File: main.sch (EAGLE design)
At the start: 45 parts, among them IC1 ATTINY13A-SSH, IC2 TP4056-42-ESOP8, IC3 LM27313XMFX_NOPB, IC4 TPL5110DDCT, IC5 ATTINY13A-SSH, T1A 2N4401, T1B NPN, X1 MINI-USB-UX60A-MB-5ST, X2 332-02

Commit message: updates
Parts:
- added R15: 0R, resistor:R-EU_R0402
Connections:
- new net N$16: IC5.PB0, R15.1
- net SOLAR_REG+/-: now also R15.2; no longer IC5.PB0
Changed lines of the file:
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@@
 <?xml version="1.0" encoding="utf-8"?>
 <!DOCTYPE eagle SYSTEM "eagle.dtd">
-<eagle version="9.5.2">
+<eagle version="9.6.0">
 <drawing>
 <settings>
@@
 <part name="GND4" library="supply1" library_urn="urn:adsk.eagle:library:371" deviceset="GND" device=""/>
 <part name="R14" library="resistor" library_urn="urn:adsk.eagle:library:348" deviceset="R-EU_" device="R0402" package3d_urn="urn:adsk.eagle:package:26058/1" value="0R"/>
+<part name="R15" library="resistor" library_urn="urn:adsk.eagle:library:348" deviceset="R-EU_" device="R0402" package3d_urn="urn:adsk.eagle:package:26058/1" value="0R"/>
 </parts>
 <sheets>
@@
 <attribute name="VALUE" x="163.83" y="59.182" size="1.778" layer="96" rot="R180"/>
 </instance>
+<instance part="R15" gate="G$1" x="170.18" y="58.42" smashed="yes" rot="R180">
+<attribute name="NAME" x="168.91" y="62.0014" size="1.778" layer="95" rot="R180"/>
+<attribute name="VALUE" x="173.99" y="61.722" size="1.778" layer="96" rot="R180"/>
+</instance>
 </instances>
 <busses>
@@
 <junction x="91.44" y="63.5"/>
 <junction x="91.44" y="58.42"/>
-<pinref part="IC5" gate="G$1" pin="PB0"/>
-<wire x1="175.26" y1="38.1" x2="175.26" y2="58.42" width="0.1524" layer="91"/>
-<wire x1="175.26" y1="58.42" x2="127" y2="58.42" width="0.1524" layer="91"/>
+<pinref part="R15" gate="G$1" pin="2"/>
+<wire x1="165.1" y1="58.42" x2="127" y2="58.42" width="0.1524" layer="91"/>
 <junction x="127" y="58.42"/>
 </segment>
@@
 </segment>
 </net>
+<net name="N$16" class="0">
+<segment>
+<pinref part="IC5" gate="G$1" pin="PB0"/>
+<wire x1="175.26" y1="38.1" x2="175.26" y2="58.42" width="0.1524" layer="91"/>
+<pinref part="R15" gate="G$1" pin="1"/>
+</segment>
+</net>

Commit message: updates
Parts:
- R14: value 0R -> 10k
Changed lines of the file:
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@@
 <part name="R13" library="resistor" library_urn="urn:adsk.eagle:library:348" deviceset="R-EU_" device="R0603" package3d_urn="urn:adsk.eagle:package:23555/2" value="1.5k"/>
 <part name="GND4" library="supply1" library_urn="urn:adsk.eagle:library:371" deviceset="GND" device=""/>
-<part name="R14" library="resistor" library_urn="urn:adsk.eagle:library:348" deviceset="R-EU_" device="R0402" package3d_urn="urn:adsk.eagle:package:26058/1" value="0R"/>
+<part name="R14" library="resistor" library_urn="urn:adsk.eagle:library:348" deviceset="R-EU_" device="R0402" package3d_urn="urn:adsk.eagle:package:26058/1" value="10k"/>
 <part name="R15" library="resistor" library_urn="urn:adsk.eagle:library:348" deviceset="R-EU_" device="R0402" package3d_urn="urn:adsk.eagle:package:26058/1" value="0R"/>
 </parts>

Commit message: rev 0.9
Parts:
- removed PAD1: (no value), wirepad:1,6/0,8
- added R16: 100R, resistor:R-EU_R0603
- C4: device rcl:C-EUC1206 -> rcl:C-EUC0805
- D1, D2: value BZX84CSMD -> (none); device diode:BZX84CSMD -> led:LEDSML0805
- R1: value 1k -> 100R
- R10: device resistor:R-EU_R0805 -> resistor:R-EU_R0603
- R13: value 1.5k -> 2.2k
- R7: device resistor:R-EU_R0603 -> resistor:R-EU_R0805
- T1B: device semicon-smd-ipc:NPN-TRANSISTOR_SOT23W -> zetex:NPNSOT23
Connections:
- new net N$17: IC5.VCC, R16.1
- net N$5: now also R16.2; no longer IC5.VCC
- net N$6: no longer PAD1.P
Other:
- moved on the sheet: R11, R13

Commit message: updates
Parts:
- removed X2: 332-02, con-garry:332-02
- added JP1: (no value), pinhead:PINHD-1X2/90
- added R17: 100R, resistor:R-EU_R0603
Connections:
- new net N$18: IC3.!SHDN, R17.2, REG1A.GND
- net SOLAR_REG+/-: now also R17.1; no longer IC3.!SHDN, REG1A.GND
- net VCC: now also JP1.2; no longer X2-1.S
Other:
- note added: "Regulator choice - TO92 or SMD"
- note added: "Safety Pin"
- moved on the sheet: C2, D1, D2, IC3, IC5, PUMP+, PUMP-, R1, R11, R12, R13, R14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

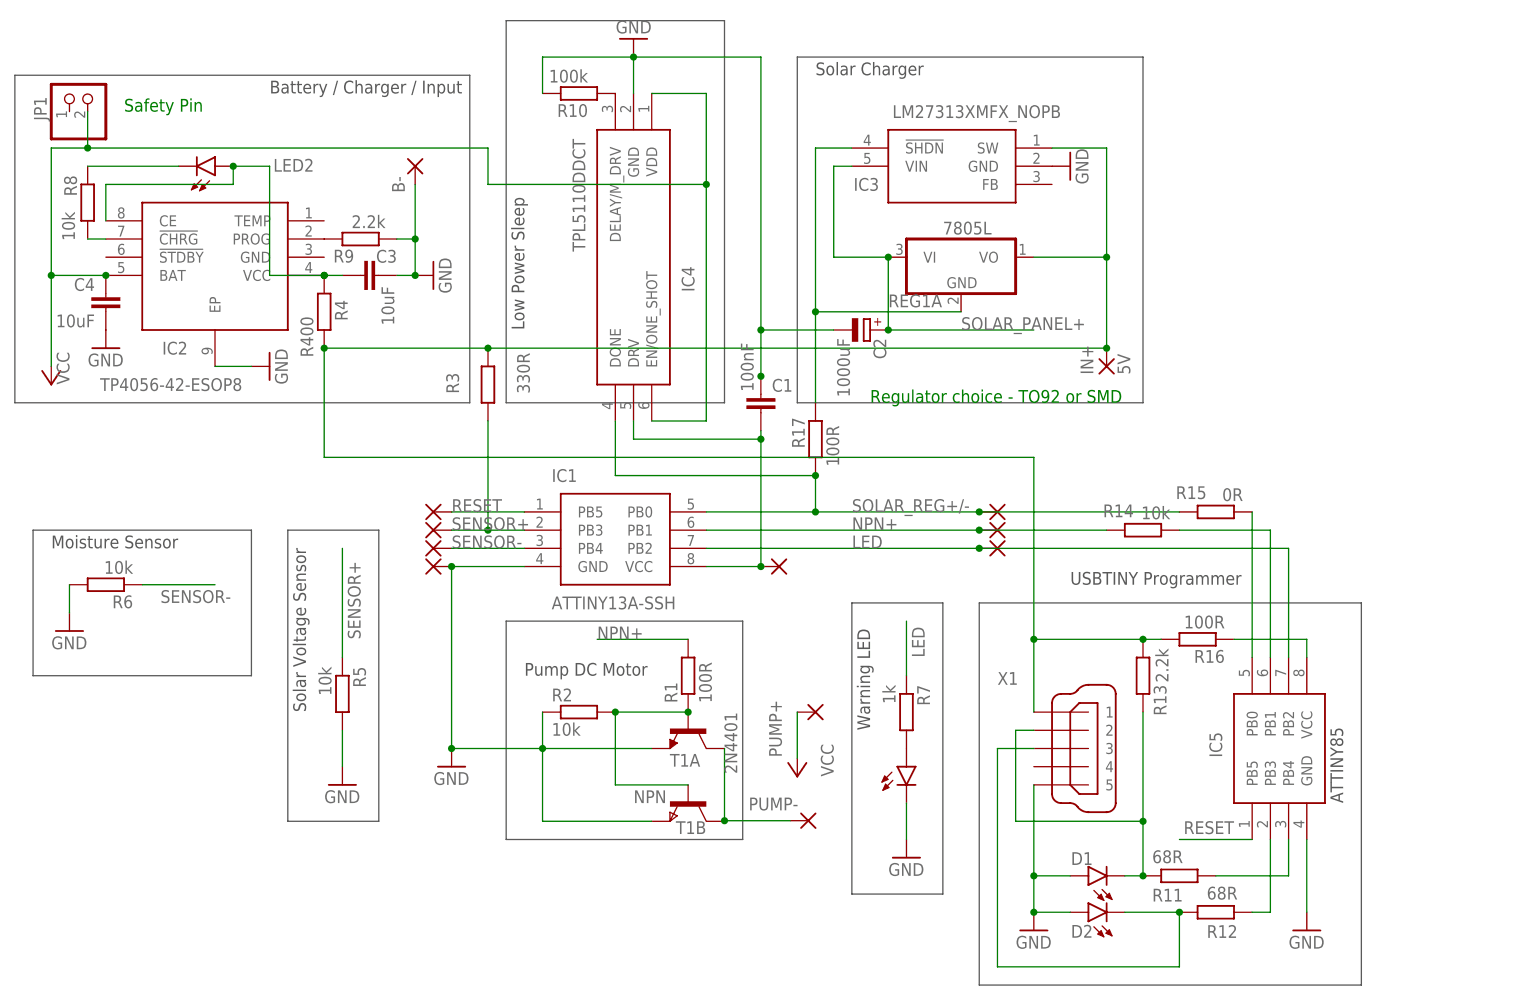
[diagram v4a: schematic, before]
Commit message: added usb diode
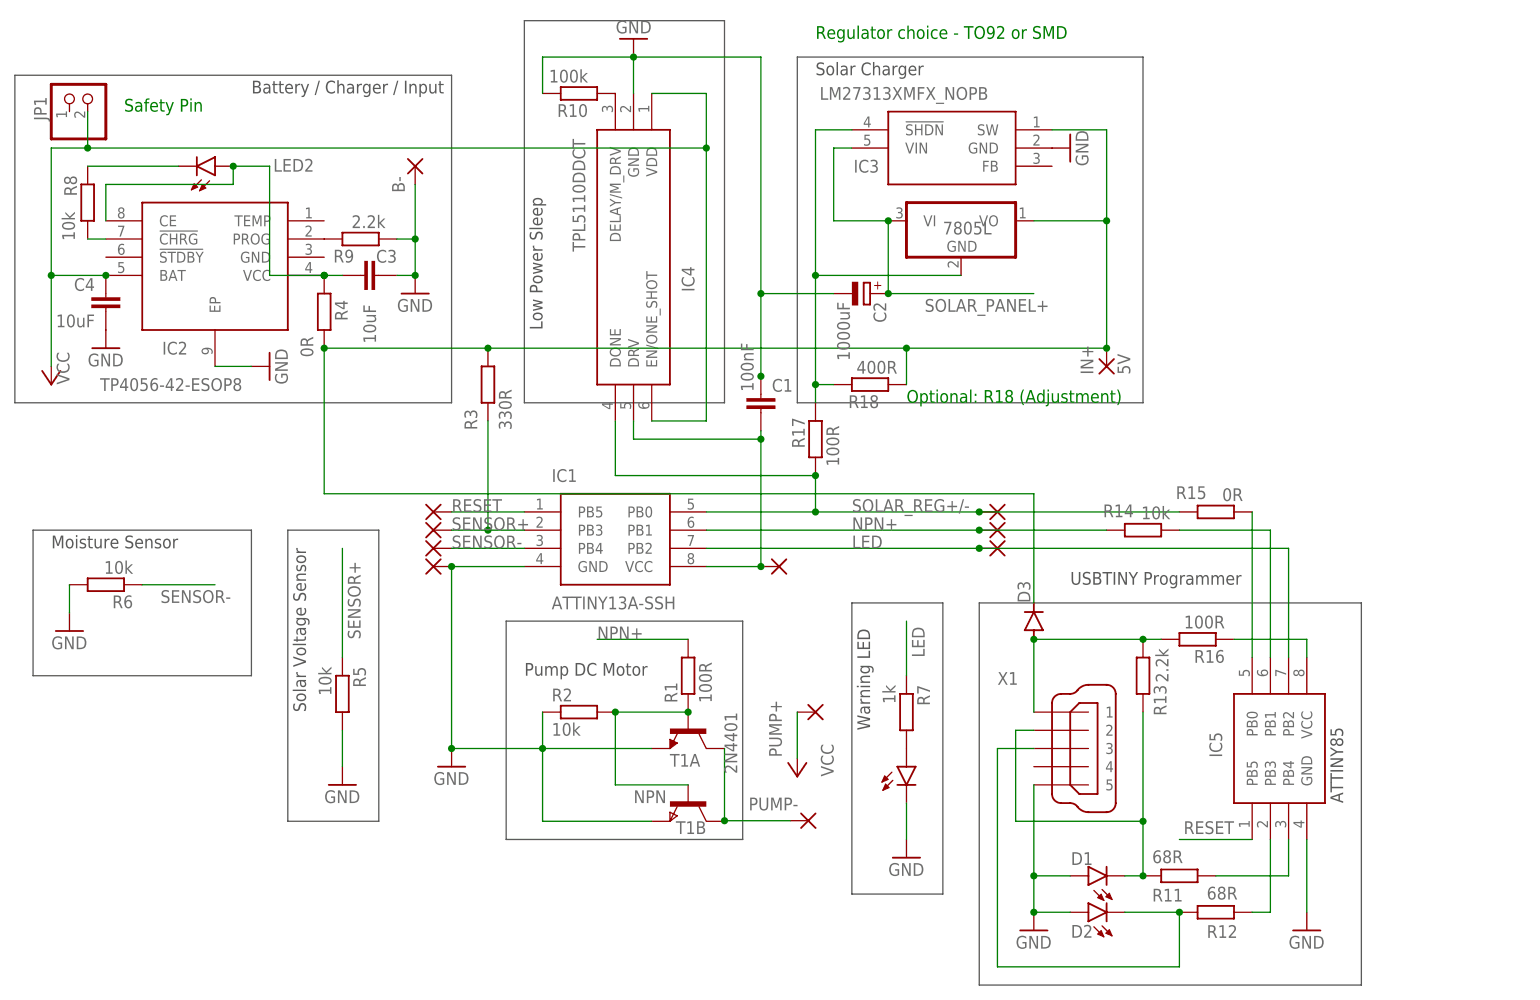
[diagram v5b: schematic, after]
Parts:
- added D3: (no value), diode:DIODE-MINIMELF
- added R18: 400R, resistor:R-EU_R0603
- R4: value R400 -> 0R
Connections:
- new net N$21: D3.A, R13.1, R16.2, X1.1
- net N$18: now also R18.2
- net N$5: now also D3.C, R18.1; no longer R13.1, R16.2, X1.1
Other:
- note added: "Optional: R18 (Adjustment)"
- moved on the sheet: C2, IC3

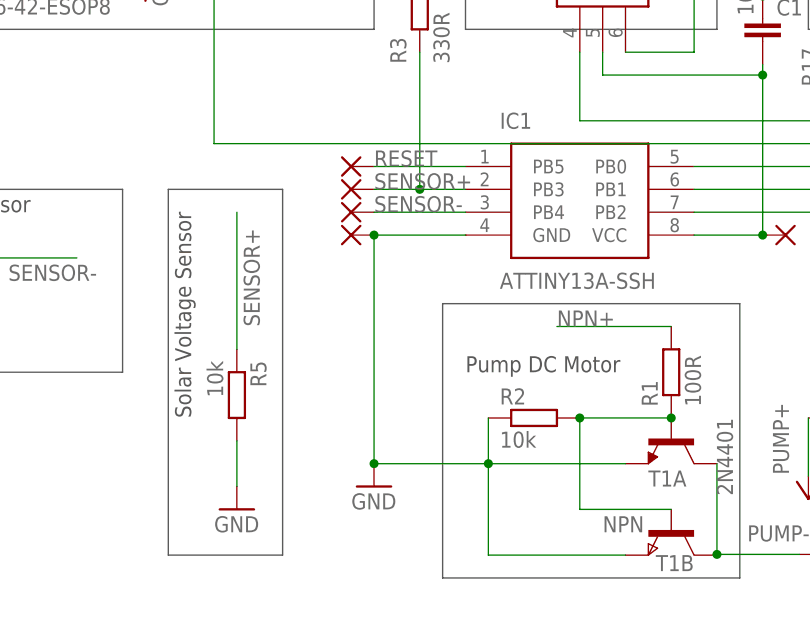
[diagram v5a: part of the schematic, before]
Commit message: reset pin filter capacitor
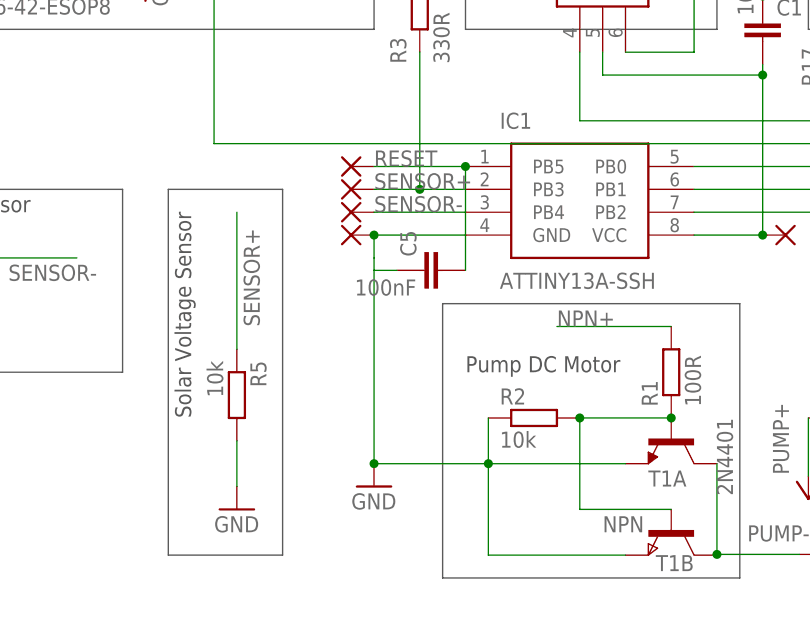
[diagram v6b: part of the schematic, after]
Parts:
- added C5: 100nF, rcl:C-EUC0805
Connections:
- net GND: now also C5.1
- net RESET: now also C5.2
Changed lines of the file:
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@@
 <grid distance="0.1" unitdist="inch" unit="inch" style="lines" multiple="1" display="no" altdistance="0.01" altunitdist="inch" altunit="inch"/>
 <layers>
-<layer number="1" name="Top" color="4" fill="1" visible="yes" active="no"/>
-<layer number="2" name="Route2" color="16" fill="1" visible="yes" active="no"/>
-<layer number="3" name="Route3" color="17" fill="1" visible="yes" active="no"/>
-<layer number="4" name="Route4" color="18" fill="1" visible="yes" active="no"/>
-<layer number="5" name="Route5" color="19" fill="1" visible="yes" active="no"/>
-<layer number="6" name="Route6" color="25" fill="1" visible="yes" active="no"/>
-<layer number="7" name="Route7" color="26" fill="1" visible="yes" active="no"/>
-<layer number="8" name="Route8" color="27" fill="1" visible="yes" active="no"/>
-<layer number="9" name="Route9" color="28" fill="1" visible="yes" active="no"/>
-<layer number="10" name="Route10" color="29" fill="1" visible="yes" active="no"/>
-<layer number="11" name="Route11" color="30" fill="1" visible="yes" active="no"/>
-<layer number="12" name="Route12" color="20" fill="1" visible="yes" active="no"/>
-<layer number="13" name="Route13" color="21" fill="1" visible="yes" active="no"/>
-<layer number="14" name="Route14" color="22" fill="1" visible="yes" active="no"/>
-<layer number="15" name="Route15" color="23" fill="1" visible="yes" active="no"/>
-<layer number="16" name="Bottom" color="1" fill="1" visible="yes" active="no"/>
-<layer number="17" name="Pads" color="2" fill="1" visible="yes" active="no"/>
-<layer number="18" name="Vias" color="2" fill="1" visible="yes" active="no"/>
-<layer number="19" name="Unrouted" color="6" fill="1" visible="yes" active="no"/>
-<layer number="20" name="Dimension" color="24" fill="1" visible="yes" active="no"/>
-<layer number="21" name="tPlace" color="7" fill="1" visible="yes" active="no"/>
-<layer number="22" name="bPlace" color="7" fill="1" visible="yes" active="no"/>
-<layer number="23" name="tOrigins" color="15" fill="1" visible="yes" active="no"/>
-<layer number="24" name="bOrigins" color="15" fill="1" visible="yes" active="no"/>
-<layer number="25" name="tNames" color="7" fill="1" visible="yes" active="no"/>
-<layer number="26" name="bNames" color="7" fill="1" visible="yes" active="no"/>
-<layer number="27" name="tValues" color="7" fill="1" visible="yes" active="no"/>
-<layer number="28" name="bValues" color="7" fill="1" visible="yes" active="no"/>
+<layer number="1" name="Top" color="4" fill="1" visible="no" active="no"/>
+<layer number="2" name="Route2" color="16" fill="1" visible="no" active="no"/>
+<layer number="3" name="Route3" color="17" fill="1" visible="no" active="no"/>
+<layer number="4" name="Route4" color="18" fill="1" visible="no" active="no"/>
+<layer number="5" name="Route5" color="19" fill="1" visible="no" active="no"/>
+<layer number="6" name="Route6" color="25" fill="1" visible="no" active="no"/>
+<layer number="7" name="Route7" color="26" fill="1" visible="no" active="no"/>
+<layer number="8" name="Route8" color="27" fill="1" visible="no" active="no"/>
+<layer number="9" name="Route9" color="28" fill="1" visible="no" active="no"/>
+<layer number="10" name="Route10" color="29" fill="1" visible="no" active="no"/>
+<layer number="11" name="Route11" color="30" fill="1" visible="no" active="no"/>
+<layer number="12" name="Route12" color="20" fill="1" visible="no" active="no"/>
+<layer number="13" name="Route13" color="21" fill="1" visible="no" active="no"/>
+<layer number="14" name="Route14" color="22" fill="1" visible="no" active="no"/>
+<layer number="15" name="Route15" color="23" fill="1" visible="no" active="no"/>
+<layer number="16" name="Bottom" color="1" fill="1" visible="no" active="no"/>
+<layer number="17" name="Pads" color="2" fill="1" visible="no" active="no"/>
+<layer number="18" name="Vias" color="2" fill="1" visible="no" active="no"/>
+<layer number="19" name="Unrouted" color="6" fill="1" visible="no" active="no"/>
+<layer number="20" name="Dimension" color="24" fill="1" visible="no" active="no"/>
+<layer number="21" name="tPlace" color="7" fill="1" visible="no" active="no"/>
+<layer number="22" name="bPlace" color="7" fill="1" visible="no" active="no"/>
+<layer number="23" name="tOrigins" color="15" fill="1" visible="no" active="no"/>
+<layer number="24" name="bOrigins" color="15" fill="1" visible="no" active="no"/>
+<layer number="25" name="tNames" color="7" fill="1" visible="no" active="no"/>
+<layer number="26" name="bNames" color="7" fill="1" visible="no" active="no"/>
+<layer number="27" name="tValues" color="7" fill="1" visible="no" active="no"/>
+<layer number="28" name="bValues" color="7" fill="1" visible="no" active="no"/>
 <layer number="29" name="tStop" color="7" fill="3" visible="no" active="no"/>
 <layer number="30" name="bStop" color="7" fill="6" visible="no" active="no"/>
@@
 <layer number="35" name="tGlue" color="7" fill="4" visible="no" active="no"/>
 <layer number="36" name="bGlue" color="7" fill="5" visible="no" active="no"/>
-<layer number="37" name="tTest" color="7" fill="1" visible="yes" active="no"/>
-<layer number="38" name="bTest" color="7" fill="1" visible="yes" active="no"/>
+<layer number="37" name="tTest" color="7" fill="1" visible="no" active="no"/>
+<layer number="38" name="bTest" color="7" fill="1" visible="no" active="no"/>
 <layer number="39" name="tKeepout" color="4" fill="11" visible="no" active="no"/>
 <layer number="40" name="bKeepout" color="1" fill="11" visible="no" active="no"/>
@@
 <layer number="44" name="Drills" color="7" fill="1" visible="no" active="no"/>
 <layer number="45" name="Holes" color="7" fill="1" visible="no" active="no"/>
-<layer number="46" name="Milling" color="3" fill="1" visible="yes" active="no"/>
-<layer number="47" name="Measures" color="7" fill="1" visible="yes" active="no"/>
-<layer number="48" name="Document" color="7" fill="1" visible="yes" active="no"/>
-<layer number="49" name="Reference" color="7" fill="1" visible="yes" active="no"/>
-<layer number="51" name="tDocu" color="7" fill="1" visible="yes" active="no"/>
-<layer number="52" name="bDocu" color="7" fill="1" visible="yes" active="no"/>
+<layer number="46" name="Milling" color="3" fill="1" visible="no" active="no"/>
+<layer number="47" name="Measures" color="7" fill="1" visible="no" active="no"/>
+<layer number="48" name="Document" color="7" fill="1" visible="no" active="no"/>
+<layer number="49" name="Reference" color="7" fill="1" visible="no" active="no"/>
+<layer number="51" name="tDocu" color="7" fill="1" visible="no" active="no"/>
+<layer number="52" name="bDocu" color="7" fill="1" visible="no" active="no"/>
 <layer number="88" name="SimResults" color="9" fill="1" visible="yes" active="yes"/>
 <layer number="89" name="SimProbes" color="9" fill="1" visible="yes" active="yes"/>
@@
 <part name="R18" library="resistor" library_urn="urn:adsk.eagle:library:348" deviceset="R-EU_" device="R0603" package3d_urn="urn:adsk.eagle:package:23555/2" value="400R"/>
 <part name="D3" library="diode" library_urn="urn:adsk.eagle:library:210" deviceset="DIODE-" device="MINIMELF" package3d_urn="urn:adsk.eagle:package:43429/2"/>
+<part name="C5" library="rcl" library_urn="urn:adsk.eagle:library:334" deviceset="C-EU" device="C0805" package3d_urn="urn:adsk.eagle:package:23617/2" value="100nF"/>
 </parts>
 <sheets>
@@
 <attribute name="VALUE" x="124.2314" y="45.72" size="1.778" layer="96" rot="R90"/>
 </instance>
+<instance part="C5" gate="G$1" x="45.72" y="46.88" smashed="yes" rot="R90">
+<attribute name="NAME" x="45.339" y="48.404" size="1.778" layer="95" rot="R90"/>
+<attribute name="VALUE" x="45.339" y="45.864" size="1.778" layer="96" rot="R180"/>
+</instance>
 </instances>
 <busses>
@@
 <wire x1="50.8" y1="50.8" x2="40.64" y2="50.8" width="0.1524" layer="91"/>
 <junction x="40.64" y="50.8"/>
-<wire x1="40.64" y1="25.4" x2="40.64" y2="50.8" width="0.1524" layer="91"/>
+<wire x1="40.64" y1="25.4" x2="40.64" y2="46.88" width="0.1524" layer="91"/>
 <pinref part="T1A" gate="G$1" pin="E"/>
+<wire x1="40.64" y1="48.26" x2="40.64" y2="50.8" width="0.1524" layer="91"/>
 <wire x1="68.58" y1="25.4" x2="53.34" y2="25.4" width="0.1524" layer="91"/>
 <junction x="40.64" y="25.4"/>
@@
 <wire x1="53.34" y1="15.24" x2="53.34" y2="25.4" width="0.1524" layer="91"/>
 <pinref part="GND3" gate="1" pin="GND"/>
+<pinref part="C5" gate="G$1" pin="1"/>
+<wire x1="40.64" y1="48.26" x2="40.64" y2="46.88" width="0.1524" layer="91"/>
+<wire x1="40.64" y1="46.88" x2="43.18" y2="46.88" width="0.1524" layer="91"/>
 </segment>
 <segment>
@@
 <label x="40.64" y="58.42" size="1.778" layer="95"/>
 <wire x1="40.64" y1="58.42" x2="50.8" y2="58.42" width="0.1524" layer="91"/>
-</segment>
-<segment>
+<pinref part="C5" gate="G$1" pin="2"/>
+<wire x1="50.8" y1="46.88" x2="50.8" y2="58.42" width="0.1524" layer="91"/>
+<junction x="50.8" y="58.42"/>
+</segment>
+<segment>
